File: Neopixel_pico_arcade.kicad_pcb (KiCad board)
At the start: 4 copper layers, 100 x 88 mm, 144 parts, among them J2 NES_controller_connector, J3 USB_C_Receptacle_USB2.0, Q1 2N7002, U1 RP2040_Stamp, U2 SN74LV1T34DBV, U3 SRV05-4HTG-D

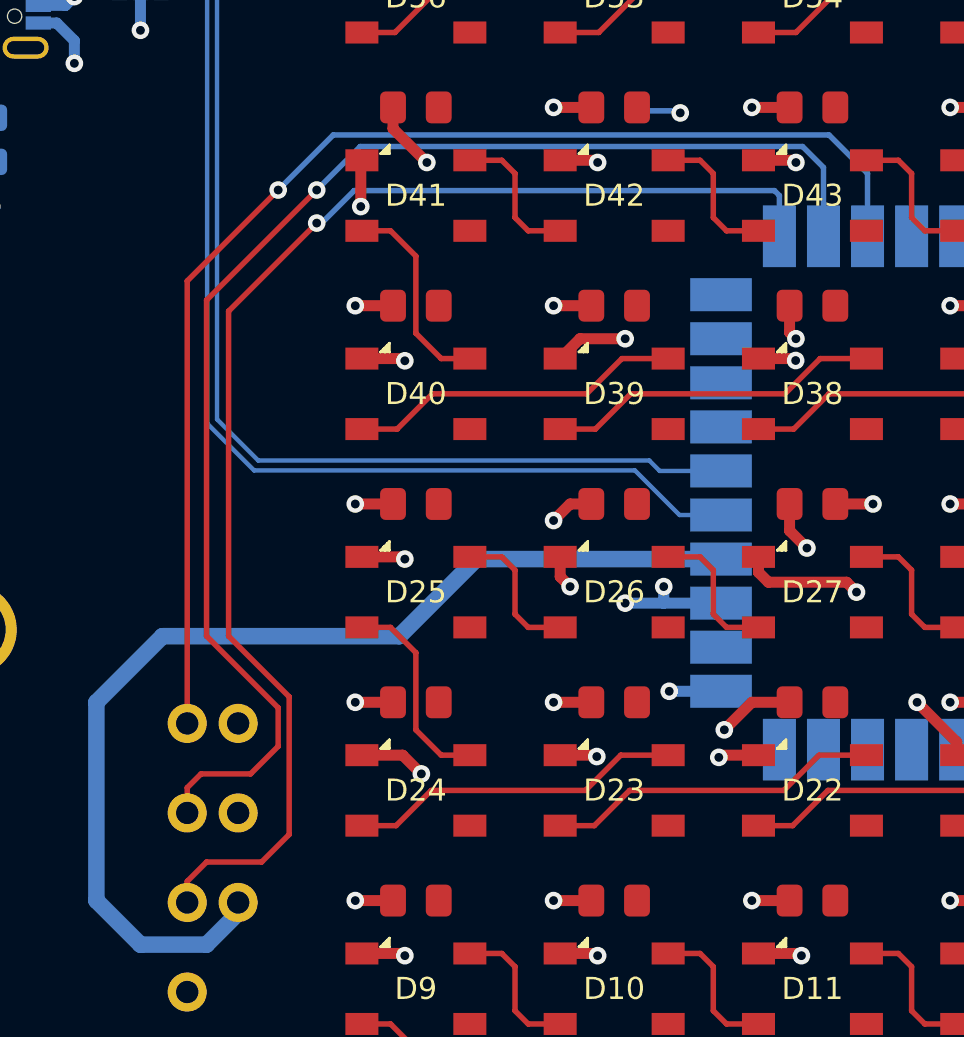
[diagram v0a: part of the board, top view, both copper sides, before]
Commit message: Reroutes NES controller data lines
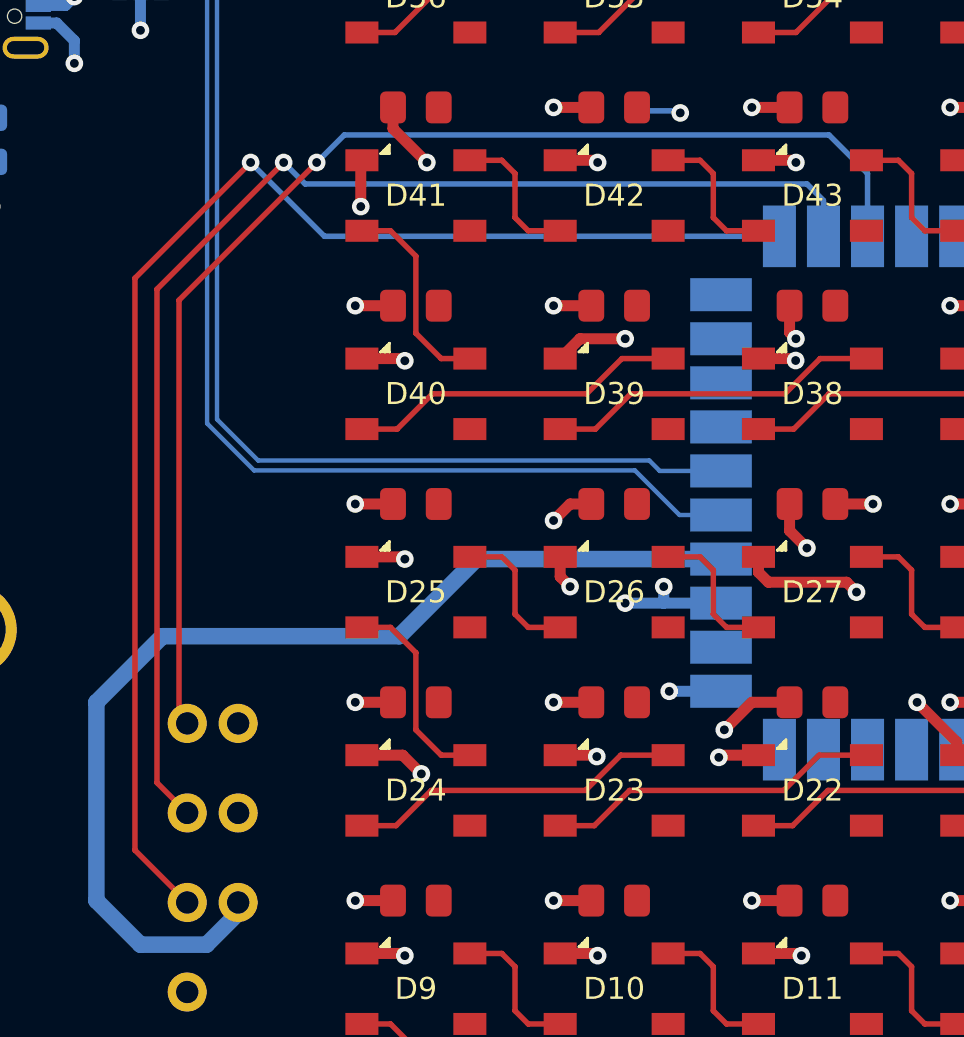
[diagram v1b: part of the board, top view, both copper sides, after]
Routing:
- net CTRL_LATCH: track 62.1 -> 59.3 mm
- net CTRL_CLK: track 61.1 -> 63.1 mm
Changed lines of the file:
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@@
   (segment (start 183 63.5) (end 183.6 64.1) (width 0.25) (layer "F.Cu") (net 68))
   (segment (start 182.4 60.9) (end 183 61.5) (width 0.25) (layer "F.Cu") (net 68))
-  (segment (start 114.12295 84.37705) (end 114.12295 104.458) (width 0.25) (layer "F.Cu") (net 70))
-  (segment (start 118.25 80.25) (end 114.12295 84.37705) (width 0.25) (layer "F.Cu") (net 70))
-  (via (at 118.25 80.25) (size 0.8) (drill 0.4) (layers "F.Cu" "B.Cu") (net 70))
+  (segment (start 113.75 104.08505) (end 114.12295 104.458) (width 0.25) (layer "F.Cu") (net 70))
+  (segment (start 113.75 85.25) (end 113.75 104.08505) (width 0.25) (layer "F.Cu") (net 70))
+  (segment (start 120 79) (end 113.75 85.25) (width 0.25) (layer "F.Cu") (net 70))
+  (via (at 120 79) (size 0.8) (drill 0.4) (layers "F.Cu" "B.Cu") (free) (net 70))
+  (segment (start 143.25 77.75) (end 121.25 77.75) (width 0.25) (layer "B.Cu") (net 70))
   (segment (start 145 79.5) (end 143.25 77.75) (width 0.25) (layer "B.Cu") (net 70))
+  (segment (start 121.25 77.75) (end 120 79) (width 0.25) (layer "B.Cu") (net 70))
   (segment (start 145 82.35) (end 145 79.5) (width 0.25) (layer "B.Cu") (net 70))
-  (segment (start 143.25 77.75) (end 120.75 77.75) (width 0.25) (layer "B.Cu") (net 70))
-  (segment (start 120.75 77.75) (end 118.25 80.25) (width 0.25) (layer "B.Cu") (net 70))
   (segment (start 110 103.5) (end 110 112.5) (width 0.75) (layer "B.Cu") (net 73))
   (segment (start 138.35 97) (end 127.25 97) (width 0.75) (layer "B.Cu") (net 73))
@@
   (segment (start 104.5 74.97) (end 103.25 76.22) (width 0.25) (layer "B.Cu") (net 78))
   (segment (start 107.3625 67.72) (end 105.75 67.72) (width 0.25) (layer "B.Cu") (net 78))
-  (segment (start 115 110.75) (end 114.12295 111.62705) (width 0.25) (layer "F.Cu") (net 80))
-  (segment (start 116 85.75) (end 116 100.5) (width 0.25) (layer "F.Cu") (net 80))
-  (segment (start 117.5 110.75) (end 115 110.75) (width 0.25) (layer "F.Cu") (net 80))
-  (segment (start 118.75 103.25) (end 118.75 109.5) (width 0.25) (layer "F.Cu") (net 80))
-  (segment (start 116 100.5) (end 118.75 103.25) (width 0.25) (layer "F.Cu") (net 80))
-  (segment (start 118.75 109.5) (end 117.5 110.75) (width 0.25) (layer "F.Cu") (net 80))
-  (segment (start 114.12295 111.62705) (end 114.12295 112.586) (width 0.25) (layer "F.Cu") (net 80))
+  (segment (start 117 79) (end 117 79.15) (width 0.25) (layer "F.Cu") (net 80))
+  (segment (start 111.75 84.25) (end 111.75 110.21305) (width 0.25) (layer "F.Cu") (net 80))
+  (segment (start 117 79) (end 111.75 84.25) (width 0.25) (layer "F.Cu") (net 80))
+  (segment (start 111.75 110.21305) (end 114.12295 112.586) (width 0.25) (layer "F.Cu") (net 80))
   (segment (start 114.12295 112.586) (end 114.664 112.586) (width 0.25) (layer "F.Cu") (net 80))
-  (segment (start 120 81.75) (end 116 85.75) (width 0.25) (layer "F.Cu") (net 80))
-  (via (at 120 81.75) (size 0.8) (drill 0.4) (layers "F.Cu" "B.Cu") (net 80))
-  (segment (start 121.699897 80.275489) (end 140.775489 80.275489) (width 0.25) (layer "B.Cu") (net 80))
-  (segment (start 120 81.75) (end 120.225386 81.75) (width 0.25) (layer "B.Cu") (net 80))
-  (segment (start 120.225386 81.75) (end 121.699897 80.275489) (width 0.25) (layer "B.Cu") (net 80))
-  (segment (start 141 80.5) (end 141 82.35) (width 0.25) (layer "B.Cu") (net 80))
-  (segment (start 140.775489 80.275489) (end 141 80.5) (width 0.25) (layer "B.Cu") (net 80))
-  (segment (start 120 80.25) (end 115 85.25) (width 0.25) (layer "F.Cu") (net 81))
-  (segment (start 117 106.75) (end 114.75 106.75) (width 0.25) (layer "F.Cu") (net 81))
-  (segment (start 118.25 103.75) (end 118.25 105.5) (width 0.25) (layer "F.Cu") (net 81))
-  (segment (start 115 100.5) (end 118.25 103.75) (width 0.25) (layer "F.Cu") (net 81))
-  (segment (start 114.75 106.75) (end 114.12295 107.37705) (width 0.25) (layer "F.Cu") (net 81))
-  (segment (start 114.12295 107.37705) (end 114.12295 108.522) (width 0.25) (layer "F.Cu") (net 81))
-  (segment (start 115 85.25) (end 115 100.5) (width 0.25) (layer "F.Cu") (net 81))
-  (segment (start 118.25 105.5) (end 117 106.75) (width 0.25) (layer "F.Cu") (net 81))
-  (via (at 120 80.25) (size 0.8) (drill 0.4) (layers "F.Cu" "B.Cu") (net 81))
-  (segment (start 121.974511 78.275489) (end 120 80.25) (width 0.25) (layer "B.Cu") (net 81))
-  (segment (start 142.050103 78.275489) (end 121.974511 78.275489) (width 0.25) (layer "B.Cu") (net 81))
-  (segment (start 143 79.225386) (end 142.050103 78.275489) (width 0.25) (layer "B.Cu") (net 81))
-  (segment (start 143 82.35) (end 143 79.225386) (width 0.25) (layer "B.Cu") (net 81))
+  (via (at 117 79) (size 0.8) (drill 0.4) (layers "F.Cu" "B.Cu") (net 80))
+  (segment (start 117 79) (end 120.35 82.35) (width 0.25) (layer "B.Cu") (net 80))
+  (segment (start 117 79) (end 117 79.25) (width 0.25) (layer "B.Cu") (net 80))
+  (segment (start 120.35 82.35) (end 141 82.35) (width 0.25) (layer "B.Cu") (net 80))
+  (segment (start 118.5 79) (end 112.75 84.75) (width 0.25) (layer "F.Cu") (net 81))
+  (segment (start 112.75 107.14905) (end 114.12295 108.522) (width 0.25) (layer "F.Cu") (net 81))
+  (segment (start 112.75 84.75) (end 112.75 107.14905) (width 0.25) (layer "F.Cu") (net 81))
+  (via (at 118.5 79) (size 0.8) (drill 0.4) (layers "F.Cu" "B.Cu") (net 81))
+  (segment (start 118.5 79) (end 119.474519 79.974519) (width 0.25) (layer "B.Cu") (net 81))
+  (segment (start 142.250867 79.974519) (end 143 80.723652) (width 0.25) (layer "B.Cu") (net 81))
+  (segment (start 119.474519 79.974519) (end 142.250867 79.974519) (width 0.25) (layer "B.Cu") (net 81))
+  (segment (start 143 80.723652) (end 143 82.35) (width 0.25) (layer "B.Cu") (net 81))
   (segment (start 159 82.35) (end 159.1 82.45) (width 0.25) (layer "B.Cu") (net 82))
   (segment (start 159.1 82.45) (end 172 82.45) (width 0.25) (layer "B.Cu") (net 82))

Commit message: Fixes most DRC errors and warnings
There are still a few errors related to the USB-C connector footprint.
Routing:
- net +5V: track 20.2 -> 18.5 mm, vias 9 -> 8
- net GND: track 260.8 -> 259.3 mm, vias 139 -> 138
- net CTRL_CLK: track 63.1 -> 62.1 mm
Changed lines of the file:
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@@
   (gr_line locked (start 103 50) (end 197 50) (layer "Edge.Cuts") (width 0.1))
   (segment (start 174 81.5) (end 182.5 81.5) (width 0.25) (layer "B.Cu") (net 1))
-  (segment (start 143.5375 94.5) (end 145.25 94.5) (width 0.5) (layer "F.Cu") (net 2))
   (via (at 135.75 98.25) (size 0.8) (drill 0.4) (layers "F.Cu" "B.Cu") (net 2))
   (via (at 117.75 57) (size 0.8) (drill 0.4) (layers "F.Cu" "B.Cu") (net 2))
@@
   (via (at 117.75 59.5) (size 0.8) (drill 0.4) (layers "F.Cu" "B.Cu") (net 2))
   (via (at 112 67) (size 0.8) (drill 0.4) (layers "F.Cu" "B.Cu") (net 2))
-  (via (at 145.25 94.5) (size 0.8) (drill 0.4) (layers "F.Cu" "B.Cu") (net 2))
   (via (at 134 99) (size 0.8) (drill 0.4) (layers "F.Cu" "B.Cu") (net 2))
   (via (at 119 58.25) (size 0.8) (drill 0.4) (layers "F.Cu" "B.Cu") (net 2))
@@
   (via (at 150.75 79) (size 0.8) (drill 0.4) (layers "F.Cu" "B.Cu") (net 4))
   (via (at 157.75 85.5) (size 0.8) (drill 0.4) (layers "F.Cu" "B.Cu") (net 4))
-  (via (at 136.5 76.75) (size 0.8) (drill 0.4) (layers "F.Cu" "B.Cu") (net 4))
   (via (at 168.737701 87.987701) (size 0.8) (drill 0.4) (layers "F.Cu" "B.Cu") (net 4))
   (via (at 139.75 58.5) (size 0.8) (drill 0.4) (layers "F.Cu" "B.Cu") (net 4))
@@
   (segment (start 188.45 120.15) (end 188.45 118.45) (width 0.5) (layer "B.Cu") (net 4))
   (segment (start 110.925 62.47) (end 109 62.47) (width 0.75) (layer "B.Cu") (net 4))
-  (segment (start 136.405 76.655) (end 136.5 76.75) (width 0.25) (layer "B.Cu") (net 4))
   (segment (start 108.2 66.27) (end 108.48 66.27) (width 0.5) (layer "B.Cu") (net 4))
   (segment (start 103.25 78.97) (end 103.25 81) (width 0.75) (layer "B.Cu") (net 4))
@@
   (segment (start 109 65.75) (end 109 64.5) (width 0.5) (layer "B.Cu") (net 4))
   (segment (start 112 71.1) (end 112 73) (width 0.5) (layer "B.Cu") (net 4))
-  (segment (start 135 76.655) (end 136.405 76.655) (width 0.25) (layer "B.Cu") (net 4))
   (segment (start 188.45 118.45) (end 188 118) (width 0.5) (layer "B.Cu") (net 4))
   (segment (start 110.925 60.42) (end 109.05 60.42) (width 0.75) (layer "B.Cu") (net 4))
@@
   (segment (start 104.5 74.97) (end 103.25 76.22) (width 0.25) (layer "B.Cu") (net 78))
   (segment (start 107.3625 67.72) (end 105.75 67.72) (width 0.25) (layer "B.Cu") (net 78))
-  (segment (start 117 79) (end 117 79.15) (width 0.25) (layer "F.Cu") (net 80))
+  (segment (start 111.75 84.25) (end 117 79) (width 0.25) (layer "F.Cu") (net 80))
   (segment (start 111.75 84.25) (end 111.75 110.21305) (width 0.25) (layer "F.Cu") (net 80))
-  (segment (start 117 79) (end 111.75 84.25) (width 0.25) (layer "F.Cu") (net 80))
   (segment (start 111.75 110.21305) (end 114.12295 112.586) (width 0.25) (layer "F.Cu") (net 80))
-  (segment (start 114.12295 112.586) (end 114.664 112.586) (width 0.25) (layer "F.Cu") (net 80))
   (via (at 117 79) (size 0.8) (drill 0.4) (layers "F.Cu" "B.Cu") (net 80))
-  (segment (start 117 79) (end 120.35 82.35) (width 0.25) (layer "B.Cu") (net 80))
-  (segment (start 117 79) (end 117 79.25) (width 0.25) (layer "B.Cu") (net 80))
   (segment (start 120.35 82.35) (end 141 82.35) (width 0.25) (layer "B.Cu") (net 80))
+  (segment (start 120.35 82.35) (end 117 79) (width 0.25) (layer "B.Cu") (net 80))
   (segment (start 118.5 79) (end 112.75 84.75) (width 0.25) (layer "F.Cu") (net 81))
   (segment (start 112.75 107.14905) (end 114.12295 108.522) (width 0.25) (layer "F.Cu") (net 81))

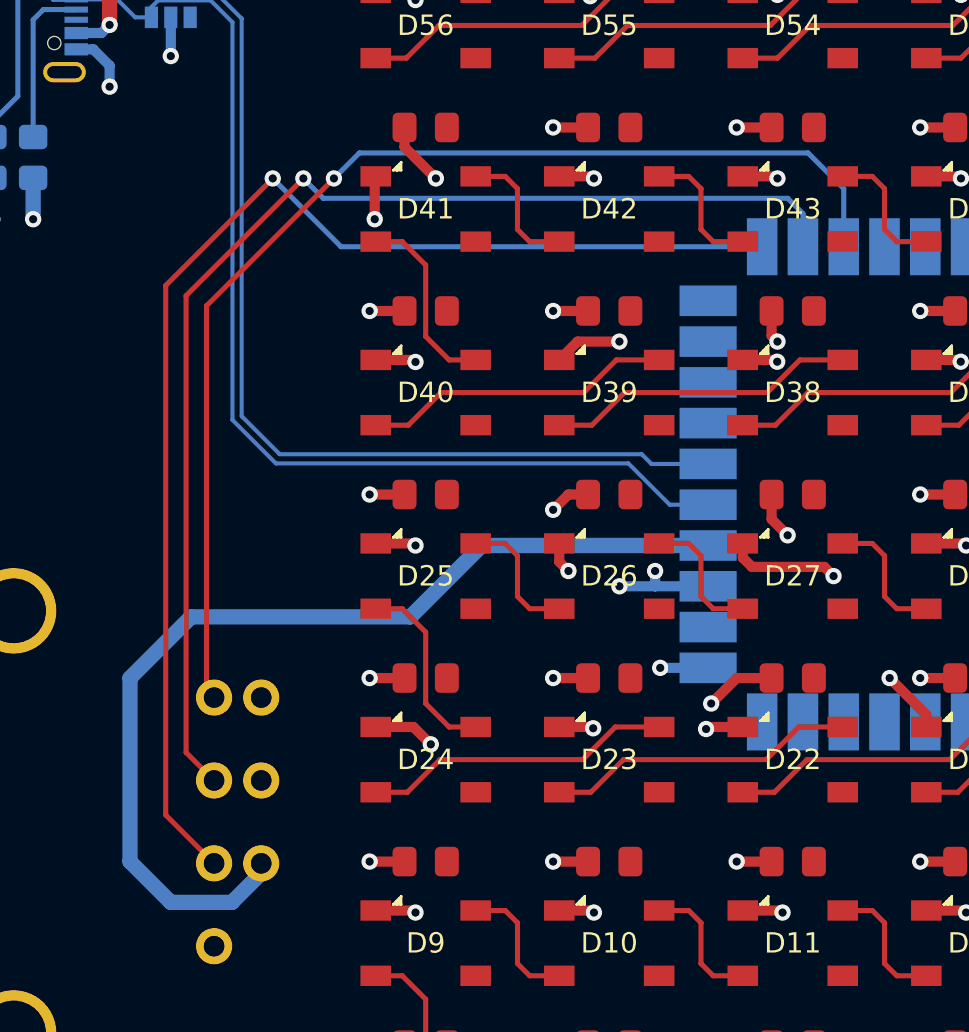
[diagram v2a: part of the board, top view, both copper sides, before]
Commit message: Reorganizes data and power lines for NES controller
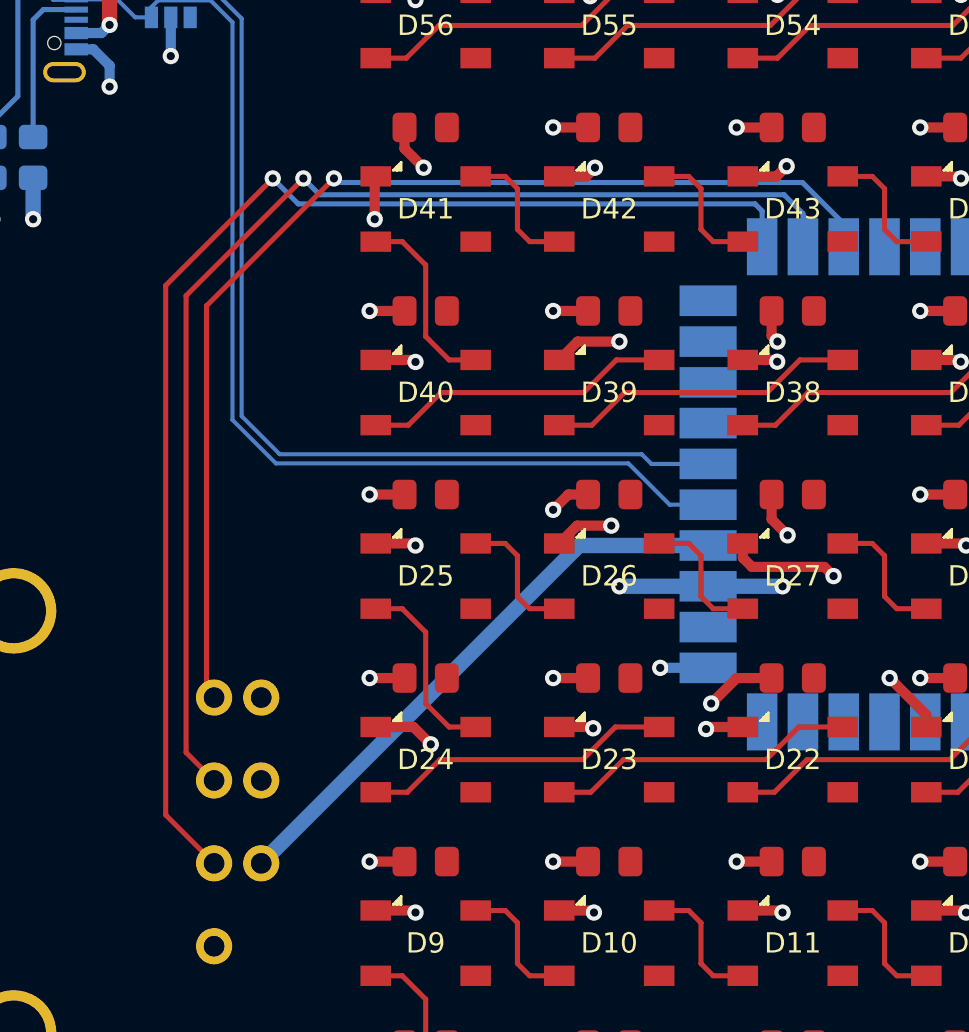
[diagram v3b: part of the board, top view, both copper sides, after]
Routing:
- net +3V3: track 48.4 -> 28.4 mm
- net +5V: track 18.5 -> 21.4 mm
- net CTRL_DATA: track 57.3 -> 55.2 mm
- net GND: track 259.3 -> 260.7 mm
- net CTRL_CLK: track 62.1 -> 63.2 mm

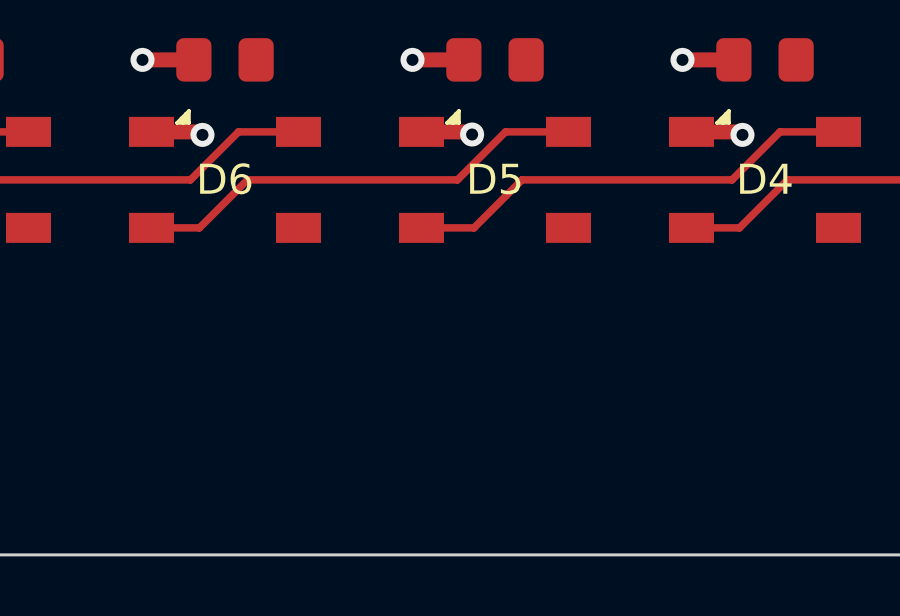
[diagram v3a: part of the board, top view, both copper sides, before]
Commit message: Adds logo footprint to the board
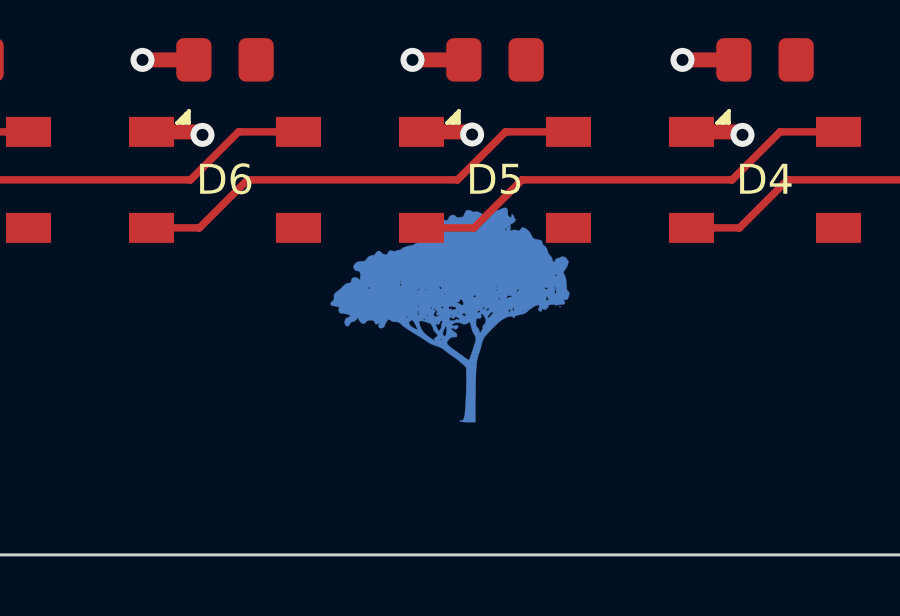
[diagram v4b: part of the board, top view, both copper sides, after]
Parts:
- added Ref**: Val**, Amieiro:url_bsilks, F.Cu at (150.0, 135.0)
- added Ref**: Val**, Amieiro:ipe_logo, F.Cu at (150.0, 130.0)

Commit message: Adds revision number (1.0) and JLCPCB order number placeholder
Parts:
- added kibuzzard-615E1A5A: G***, kibuzzard-615E1A5A, B.Cu at (150.0, 53.0)
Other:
- board text added: "JLCJLCJLCJLC"
